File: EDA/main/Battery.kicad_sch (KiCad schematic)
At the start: 38 parts, among them U10 TPS25730DREFR, U11 STM32L031G6U6, U9 BQ25895RTWT, Y1 ABS07-32.768KHZ-T

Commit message: Project restructure, and added a bottom assembly PCB.
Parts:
- C12, C13, C14, C16, C17, C25, C26, C27, C28: footprint (none) -> Capacitor_SMD:C_0402_1005Metric
- C15, C18, C19, C20, C21, C22, C23, C24, C29, C30: footprint (none) -> Capacitor_SMD:C_0603_1608Metric
- R10, R13, R14, R15, R16, R17, R25: footprint (none) -> Resistor_SMD:R_0603_1608Metric
- R18, R19, R20, R21, R22, R23, R24, R26: footprint (none) -> Resistor_SMD:R_0402_1005Metric
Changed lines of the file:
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@@
 			)
 		)
-		(property "Footprint" ""
+		(property "Footprint" "Capacitor_SMD:C_0603_1608Metric"
 			(at 281.6352 125.73 0)
 			(effects
@@
 			)
 		)
-		(property "Footprint" ""
+		(property "Footprint" "Resistor_SMD:R_0603_1608Metric"
 			(at 339.598 236.22 90)
 			(effects
@@
 			)
 		)
-		(property "Footprint" ""
+		(property "Footprint" "Resistor_SMD:R_0603_1608Metric"
 			(at 339.598 226.06 90)
 			(effects
@@
 			)
 		)
-		(property "Footprint" ""
+		(property "Footprint" "Capacitor_SMD:C_0603_1608Metric"
 			(at 275.2852 166.37 0)
 			(effects
@@
 			)
 		)
-		(property "Footprint" ""
+		(property "Footprint" "Capacitor_SMD:C_0402_1005Metric"
 			(at 263.8552 138.43 0)
 			(effects
@@
 			)
 		)
-		(property "Footprint" ""
+		(property "Footprint" "Capacitor_SMD:C_0402_1005Metric"
 			(at 270.2052 138.43 0)
 			(effects
@@
 			)
 		)
-		(property "Footprint" ""
+		(property "Footprint" "Resistor_SMD:R_0402_1005Metric"
 			(at 98.298 87.63 90)
 			(effects
@@
 			)
 		)
-		(property "Footprint" ""
+		(property "Footprint" "Capacitor_SMD:C_0603_1608Metric"
 			(at 284.1752 168.91 0)
 			(effects
@@
 			)
 		)
-		(property "Footprint" ""
+		(property "Footprint" "Resistor_SMD:R_0402_1005Metric"
 			(at 36.068 88.9 90)
 			(effects
@@
 			)
 		)
-		(property "Footprint" ""
+		(property "Footprint" "Resistor_SMD:R_0402_1005Metric"
 			(at 261.112 199.39 90)
 			(effects
@@
 			)
 		)
-		(property "Footprint" ""
+		(property "Footprint" "Capacitor_SMD:C_0402_1005Metric"
 			(at 142.24 267.0048 0)
 			(effects
@@
 			)
 		)
-		(property "Footprint" ""
+		(property "Footprint" "Resistor_SMD:R_0603_1608Metric"
 			(at 300.228 236.22 90)
 			(effects
@@
 			)
 		)
-		(property "Footprint" ""
+		(property "Footprint" "Capacitor_SMD:C_0603_1608Metric"
 			(at 261.3152 156.21 0)
 			(effects
@@
 			)
 		)
-		(property "Footprint" ""
+		(property "Footprint" "Resistor_SMD:R_0402_1005Metric"
 			(at 28.448 88.9 90)
 			(effects
@@
 			)
 		)
-		(property "Footprint" ""
+		(property "Footprint" "Capacitor_SMD:C_0603_1608Metric"
 			(at 98.7552 248.92 0)
 			(effects
@@
 			)
 		)
-		(property "Footprint" ""
+		(property "Footprint" "Capacitor_SMD:C_0603_1608Metric"
 			(at 267.6652 156.21 0)
 			(effects
@@
 			)
 		)
-		(property "Footprint" ""
+		(property "Footprint" "Resistor_SMD:R_0603_1608Metric"
 			(at 36.068 132.08 90)
 			(effects
@@
 			)
 		)
-		(property "Footprint" ""
+		(property "Footprint" "Capacitor_SMD:C_0603_1608Metric"
 			(at 254.9652 156.21 0)
 			(effects
@@
 			)
 		)
-		(property "Footprint" ""
+		(property "Footprint" "Capacitor_SMD:C_0402_1005Metric"
 			(at 356.5652 167.64 0)
 			(effects
@@
 			)
 		)
-		(property "Footprint" ""
+		(property "Footprint" "Capacitor_SMD:C_0402_1005Metric"
 			(at 142.24 277.1648 0)
 			(effects
@@
 			)
 		)
-		(property "Footprint" ""
+		(property "Footprint" "Capacitor_SMD:C_0603_1608Metric"
 			(at 88.5952 48.26 0)
 			(effects
@@
 			)
 		)
-		(property "Footprint" ""
+		(property "Footprint" "Capacitor_SMD:C_0402_1005Metric"
 			(at 108.9152 236.22 0)
 			(effects
@@
 			)
 		)
-		(property "Footprint" ""
+		(property "Footprint" "Resistor_SMD:R_0402_1005Metric"
 			(at 253.492 199.39 90)
 			(effects
@@
 			)
 		)
-		(property "Footprint" ""
+		(property "Footprint" "Resistor_SMD:R_0603_1608Metric"
 			(at 319.278 236.22 90)
 			(effects
@@
 			)
 		)
-		(property "Footprint" ""
+		(property "Footprint" "Resistor_SMD:R_0603_1608Metric"
 			(at 300.228 226.06 90)
 			(effects
@@
 			)
 		)
-		(property "Footprint" ""
+		(property "Footprint" "Capacitor_SMD:C_0402_1005Metric"
 			(at 364.1852 167.64 0)
 			(effects
@@
 			)
 		)
-		(property "Footprint" ""
+		(property "Footprint" "Resistor_SMD:R_0402_1005Metric"
 			(at 278.13 182.372 90)
 			(effects
@@
 			)
 		)
-		(property "Footprint" ""
+		(property "Footprint" "Capacitor_SMD:C_0603_1608Metric"
 			(at 257.5052 138.43 0)
 			(effects
@@
 			)
 		)
-		(property "Footprint" ""
+		(property "Footprint" "Capacitor_SMD:C_0402_1005Metric"
 			(at 276.5552 138.43 0)
 			(effects
@@
 			)
 		)
-		(property "Footprint" ""
+		(property "Footprint" "Resistor_SMD:R_0603_1608Metric"
 			(at 319.278 226.06 90)
 			(effects
@@
 			)
 		)
-		(property "Footprint" ""
+		(property "Footprint" "Capacitor_SMD:C_0402_1005Metric"
 			(at 106.3752 248.92 0)
 			(effects
@@
 			)
 		)
-		(property "Footprint" ""
+		(property "Footprint" "Capacitor_SMD:C_0603_1608Metric"
 			(at 101.2952 236.22 0)
 			(effects
@@
 			)
 		)
-		(property "Footprint" ""
+		(property "Footprint" "Resistor_SMD:R_0402_1005Metric"
 			(at 278.13 200.152 90)
 			(effects
@@
 			)
 		)
-		(property "Footprint" ""
+		(property "Footprint" "Resistor_SMD:R_0402_1005Metric"
 			(at 278.13 202.692 90)
 			(effects

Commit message: Assigned CS and INT from sensors, and added SWD to PWR-MCU and CORE-MCU
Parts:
- added J5: STM32L0_SWD, CANSAT-lib:TAG-CONNECT_TC2050-IDC, symbol CANSAT-lib:TC2050-IDC
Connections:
- net 3V3: now also J5.1
- net GND: now also J5.3, J5.5
- net SWDIO: now reaches U11.21 (PA13)
- net SWDIO: now also J5.2
- net SWCLK: now reaches U11.22 (PA14)
- net SWCLK: now also J5.4
- net NRST: now reaches U11.4 (NRST)
- net NRST: now also J5.6
- no-connect marks 5 -> 9

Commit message: Uploaded work
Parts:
- added C100, C91, C95: 4.7uF, Capacitor_SMD:C_0603_1608Metric, symbol Device:C
- added C101, C102, C103, C105, C92, C94: 10uF, Capacitor_SMD:C_0603_1608Metric, symbol Device:C
- added C104, C87, C88, C97: 100nF, Capacitor_SMD:C_0402_1005Metric, symbol Device:C
- added C89, C96: 1uF, Capacitor_SMD:C_0603_1608Metric, symbol Device:C
- added C90, C93: 22uF, Capacitor_SMD:C_0603_1608Metric, symbol Device:C
- added C98: 10pF, Capacitor_SMD:C_0402_1005Metric, symbol Device:C
- added C99: 47nF, Capacitor_SMD:C_0402_1005Metric, symbol Device:C
- added J7: SKRPACE010, CANSAT-lib:SW_SKRPACE010_AAL, symbol CANSAT-lib:SKRPACE010
- added J8: Power, CANSAT-lib:SW_SKRPACE010_AAL, symbol CANSAT-lib:SKRPACE010
- added J9: XT30 Battery, CANSAT-lib:AMASS_XT30PW-M, symbol CANSAT-lib:XT30PW-M
- added L1: 1uH, symbol Device:L
- added L2: 2.2uH, symbol Device:L
- added R30: 10kΩ, Resistor_SMD:R_0402_1005Metric, symbol Device:R
- added R31: 560kΩ, Resistor_SMD:R_0402_1005Metric, symbol Device:R
- added R32: 100kΩ, Resistor_SMD:R_0402_1005Metric, symbol Device:R
- added S1: Main Switch, CANSAT-lib:SW_500SSP1S1M6QEA, symbol CANSAT-lib:500SSP1S1M6QEA
- added U1: TPS63060DSCT, CANSAT-lib:CONV_TPS63060DSCT, symbol CANSAT-lib:TPS63060DSCT
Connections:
- net PWR_MCU_3V3 is gone; now on net 3V3: C27.1, C28.2, C29.2, C30.1, U11.1 (VDD), U11.17 (VDD), U11.5 (VDDA)
- net 3V3: now also C93.1, C94.1, C95.1, C96.1, C97.1, J7.2, R31.1, U1.9 (VOUT)
- net GND: now also C100.2, C101.2, C102.2, C103.2, C104.2, C105.2, C87.2, C88.2, C89.2, C90.2, C91.2, C92.2, C93.2, C94.2, C95.2, C96.2, C97.2, C98.2, J8.3, J9.N, R30.2, R32.2, U1.11 (PGND), U1.4 (PS/SYNC), U1.7 (GND)
- net SPI_CS_PWR-MCU: now reaches U11.10 (PA4)
- net SPI_SCK: now reaches U11.11 (PA5)
- net SPI_SDO: now reaches U11.12 (PA6)
- net SPI_SDI: now reaches U11.13 (PA7)
- net BOOT0: now reaches U11.27 (BOOT0)
- net BOOT0: now also J7.3, R30.1
- net at U9.12 (~{QON}): now also C104.1, J8.2
- net at U9.13 (BAT_13): now also U9.14 (BAT_14), S1.2
- net SYS: now reaches U9.15 (SYS_15)
- net SYS: now also U9.16 (SYS_16), C101.1, C102.1, C88.1, C89.1, C90.1, C91.1, C92.1, L2.2, U1.2 (VIN), U1.3 (EN)
- net at U9.19 (SW_19): now also U9.20 (SW_20), C99.1, L2.1
- net at U9.21 (BTST): now also C99.2
- net at U9.22 (REGN): now also C100.1
- net at U9.23 (PMID): now also C103.1
- new net: C105.1, J9.P, S1.1
- new net: L1.2, U1.1 (L1)
- new net: L1.1, U1.10 (L2)
- new net: C87.1, U1.6 (VAUX)
- new net: C98.1, R31.2, R32.1, U1.8 (FB)
- no-connect marks 9 -> 13
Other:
- note added: "3.3V Rail"
- note added: "Battery monitoring"
- note added: "Power management MCU"
- moved on the sheet: C24, C25, C26, C27, C28, C29, C30, J5, R23, R24, R25, R26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

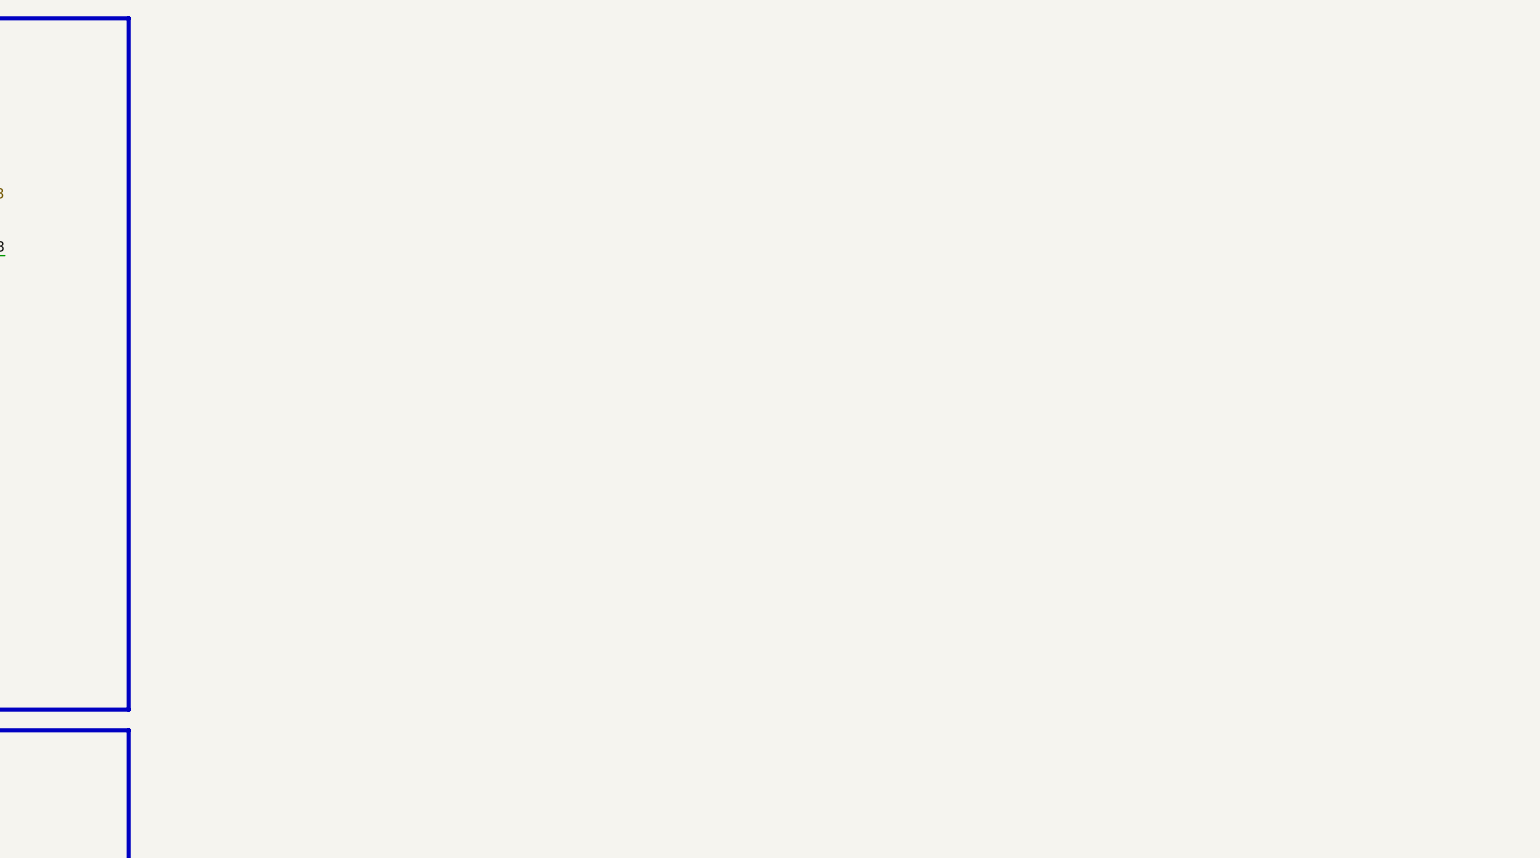
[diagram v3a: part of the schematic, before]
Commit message: Added GNSS and SIM800L
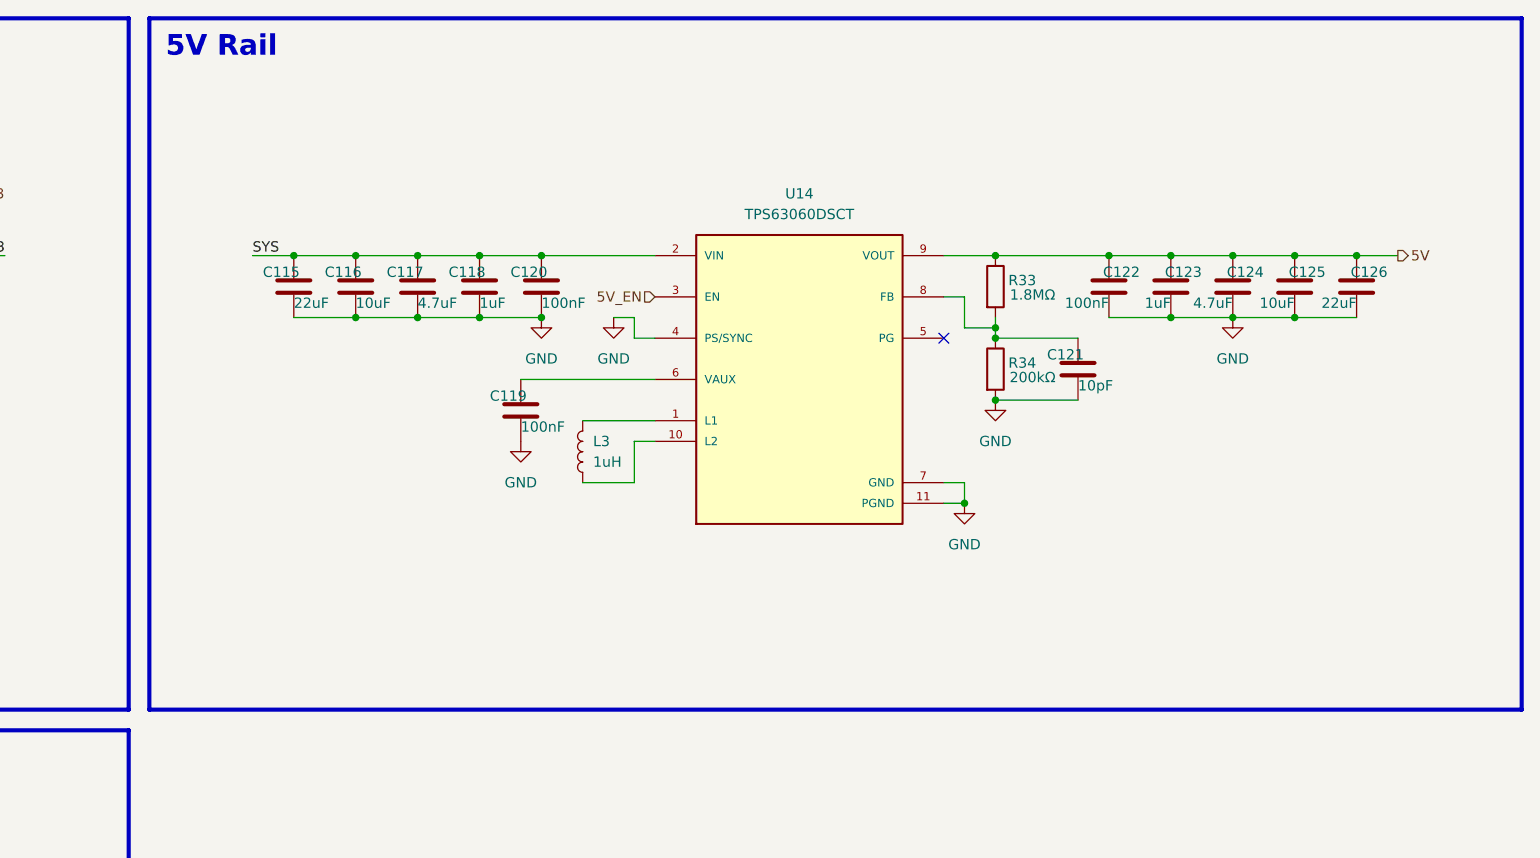
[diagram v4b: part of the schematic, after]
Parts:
- added C115, C126: 22uF, Capacitor_SMD:C_0603_1608Metric, symbol Device:C
- added C116, C125: 10uF, Capacitor_SMD:C_0603_1608Metric, symbol Device:C
- added C117, C124: 4.7uF, Capacitor_SMD:C_0603_1608Metric, symbol Device:C
- added C118, C123: 1uF, Capacitor_SMD:C_0603_1608Metric, symbol Device:C
- added C119, C120, C122: 100nF, Capacitor_SMD:C_0402_1005Metric, symbol Device:C
- added C121: 10pF, Capacitor_SMD:C_0402_1005Metric, symbol Device:C
- added L3: 1uH, symbol Device:L
- added R33: 1.8MΩ, Resistor_SMD:R_0402_1005Metric, symbol Device:R
- added R34: 200kΩ, Resistor_SMD:R_0402_1005Metric, symbol Device:R
- added U14: TPS63060DSCT, CANSAT-lib:CONV_TPS63060DSCT, symbol CANSAT-lib:TPS63060DSCT
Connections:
- net GND: now also C115.2, C116.2, C117.2, C118.2, C119.2, C120.2, C121.2, C122.2, C123.2, C124.2, C125.2, C126.2, R34.2, U14.11 (PGND), U14.4 (PS/SYNC), U14.7 (GND)
- net SYS: now also C115.1, C116.1, C117.1, C118.1, C120.1, U14.2 (VIN)
- new net: C121.1, R33.2, R34.1, U14.8 (FB)
- new net: L3.2, U14.1 (L1)
- new net: L3.1, U14.10 (L2)
- new net: C119.1, U14.6 (VAUX)
- new net 5V: C122.1, C123.1, C124.1, C125.1, C126.1, R33.1, U14.9 (VOUT)
- new net 5V_EN: U14.3 (EN)
- no-connect marks 13 -> 14
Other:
- note added: "5V Rail"

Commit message: Uploaded work
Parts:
- L1, L3: footprint (none) -> Inductor_SMD:L_1008_2520Metric; Manufacturer Part (none) -> 74438324010
- L2: footprint (none) -> Inductor_SMD:L_Wuerth_MAPI-4020; Manufacturer Part (none) -> 74438356022
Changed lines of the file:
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@@
 	(rectangle
 		(start 64.77 130.81)
-		(end 233.68 251.46)
+		(end 233.68 250.19)
 		(stroke
 			(width 0.508)
@@
 			)
 		)
-		(property "Footprint" ""
+		(property "Footprint" "Inductor_SMD:L_Wuerth_MAPI-4020"
 			(at 186.69 54.61 0)
 			(effects
@@
 			)
 		)
+		(property "Manufacturer Part" "74438356022"
+			(at 186.69 54.61 90)
+			(effects
+				(font
+					(size 1.27 1.27)
+				)
+				(hide yes)
+			)
+		)
 		(pin "1"
 		)
@@
 			)
 		)
-		(property "Footprint" ""
+		(property "Footprint" "Inductor_SMD:L_1008_2520Metric"
 			(at 289.56 68.58 0)
 			(effects
@@
 			)
 		)
+		(property "Manufacturer Part" "74438324010"
+			(at 289.56 68.58 0)
+			(effects
+				(font
+					(size 1.27 1.27)
+				)
+				(hide yes)
+			)
+		)
 		(pin "1"
 		)
@@
 			)
 		)
-		(property "Footprint" ""
+		(property "Footprint" "Inductor_SMD:L_1008_2520Metric"
 			(at 461.01 68.58 0)
 			(effects
@@
 			(at 461.01 68.58 0)
 			(effects
+				(font
+					(size 1.27 1.27)
+				)
+				(hide yes)
+			)
+		)
+		(property "Manufacturer Part" "74438324010"
+			(at 461.01 68.58 0)
+			(effects

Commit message: PCB done
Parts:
- removed C115, C126: 22uF, Capacitor_SMD:C_0603_1608Metric, symbol Device:C
- removed C116, C125: 10uF, Capacitor_SMD:C_0603_1608Metric, symbol Device:C
- removed C117, C124: 4.7uF, Capacitor_SMD:C_0603_1608Metric, symbol Device:C
- removed C118, C123: 1uF, Capacitor_SMD:C_0603_1608Metric, symbol Device:C
- removed C119, C120, C122: 100nF, Capacitor_SMD:C_0402_1005Metric, symbol Device:C
- removed C121: 10pF, Capacitor_SMD:C_0402_1005Metric, symbol Device:C
- removed L3: 1uH, Inductor_SMD:L_1008_2520Metric, symbol Device:L
- removed R33: 1.8MΩ, Resistor_SMD:R_0402_1005Metric, symbol Device:R
- removed R34: 200kΩ, Resistor_SMD:R_0402_1005Metric, symbol Device:R
- removed U14: TPS63060DSCT, CANSAT-lib:CONV_TPS63060DSCT, symbol CANSAT-lib:TPS63060DSCT
- added R27, R28: 10kΩ, Resistor_SMD:R_0402_1005Metric, symbol Device:R
- C100, C15, C22, C91, C95: Manufacturer Part (none) -> CL10A475KP8NNNC
- C101, C102, C103, C105, C18, C21, C23, C29, C92, C94: Manufacturer Part (none) -> CL10X106MO8NRNC
- C104, C27, C28, C87, C88, C97: Manufacturer Part (none) -> CL05B104KP5NNNC
- C12, C13, C14: Manufacturer Part (none) -> CL05B103KB5NNNC
- C16, C17: Manufacturer Part (none) -> CL05C331JB5NNNC
- C19, C20, C90, C93: Manufacturer Part (none) -> CL10A226MP8NUNE
- C24, C30, C89, C96: Manufacturer Part (none) -> CL10B105MO8NNWC
- C25, C26, C98: Manufacturer Part (none) -> CL05C100JB5NNNC
- C99: Manufacturer Part (none) -> CL05B473KB5VPNC
- J7, J8: Manufacturer Part (none) -> SKRPACE010
- R10, R14, R16: Manufacturer Part (none) -> RC0603JR-07200KL
- R13, R15: Manufacturer Part (none) -> RC0603FR-07100KL
- R17: Manufacturer Part (none) -> RC0603FR-1027KL
- R18, R19, R20, R23, R24, R26, R30: Manufacturer Part (none) -> RC0402FR-0710KL
- R21, R22: Manufacturer Part (none) -> RC0402FR-073K3L
- R25: Manufacturer Part (none) -> RC0603FR-07150RL
- R31: Manufacturer Part (none) -> RC0402FR-13560KL
- R32: Manufacturer Part (none) -> RC0402FR-07100KL
- S1: Manufacturer Part (none) -> 500SSP1S1M6QEA
- U1: Manufacturer Part (none) -> TPS63060MDSCTEP
- U10: Manufacturer Part (none) -> TPS25730DREFR
- U11: Manufacturer Part (none) -> STM32L031G6U6
- U9: Manufacturer Part (none) -> BQ25895RTWT
- Y1: Manufacturer Part (none) -> ABS07-32.768KHZ-T
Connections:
- net BAT_INT is gone; now on net BQ_INT: R26.1, U9.7 (INT)
- net BAT_TS: now also R27.2, R28.1
- net GND: now also R28.2
- net BQ_INT: now reaches U11.23 (PA15)
- net REGN: now reaches C100.1, U9.22 (REGN)
- net REGN: now also R27.1
- no-connect marks 14 -> 13
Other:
- note removed: "5V Rail"
